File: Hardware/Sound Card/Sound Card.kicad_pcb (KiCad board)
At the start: 2 copper layers, 100 x 57.6 mm, 38 parts, among them J1 ICSP, J2 6502 Card Edge, J3 Conn_02x08_Odd_Even, J4 PORT A, J5 3.5mm TRS, U1 ATmega328P-A, U2 74HC245, U3 74HC245, U4 74HC138, U5 AY-3-8912, U6 LM386, X1 2 MHz, Y1 16MHz

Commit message: Add Wozmon
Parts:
- removed C10, C2, C5, C6: 100nF, Capacitor_SMD:C_0805_2012Metric
- removed C11: 470nF, Capacitor_SMD:C_0805_2012Metric
- removed C3, C4: 22pF, Capacitor_SMD:C_0805_2012Metric
- removed R4, R5, R6: 1k, Resistor_SMD:R_0805_2012Metric
- removed R7: 10, Resistor_SMD:R_0805_2012Metric
- removed U2, U3: 74HC245, Package_SO:SOIC-20W_7.5x12.8mm_P1.27mm
- removed U6: LM386, Package_SO:SOP-8_3.76x4.96mm_P1.27mm
- removed Y1: 16MHz, Crystal:Crystal_HC49-U_Vertical
- added JP1: SolderJumper_2_Bridged, Jumper:SolderJumper-2_P1.3mm_Bridged_RoundedPad1.0x1.5mm, F.Cu at (92.5, 110.2)
- D1: value 1N4001 -> D_Schottky; footprint Diode_SMD:D_SMA -> Diode_THT:D_DO-35_SOD27_P7.62mm_Horizontal
- J1: value ICSP -> Audio Out; footprint Connector_PinHeader_2.54mm:PinHeader_2x03_P2.54mm_Vertical -> Connector_JST:JST_XH_B2B-XH-A_1x02_P2.50mm_Vertical
- U1: value ATmega328P-A -> 65C22; footprint Package_QFP:TQFP-32_7x7mm_P0.8mm -> Package_DIP:DIP-40_W15.24mm_Socket_LongPads
- moved C1 48.9 mm to (86.1, 98.9)
- moved C8 44.6 mm to (86.1, 101.9)
- moved C9 44.6 mm to (86.1, 104.9)
- moved U1 44.4 mm to (43.6, 73.2)
- moved TP1 36.9 mm to (82.1, 99.2)
- moved TP2 36.9 mm to (82.1, 102.7)
- moved TP3 36.9 mm to (82.1, 106.2)
- moved R1 32.7 mm to (90.5, 98.8)
- moved R2 32.7 mm to (90.5, 101.8)
- moved R3 32.7 mm to (90.5, 104.8)
- moved J5 32.1 mm to (87.3, 79.5)
- moved U5 24.5 mm to (63.0, 73.2)
- moved J4 24.3 mm to (85.5, 110.7)
- moved X1 22.8 mm to (64.4, 119.3)
- moved J1 15.0 mm to (82.6, 89.0)
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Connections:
- C9 pad 2: Net-(U6-+) -> Net-(J1-Pin_1)
- D1 pad 1: GND -> Net-(D1-K)
- D1 pad 2: Net-(D1-A) -> IRQB
- J1 pad 1: MISO -> Net-(J1-Pin_1)
- J1 pad 2: VCC -> GND
- J2 pad IRQB: unconnected-(J2-PadIRQB) -> IRQB
- J2 pad RWB: MISO -> RWB
- J4 pad 11: unconnected-(J4-Pin_11-Pad11) -> CA1
- J4 pad 12: unconnected-(J4-Pin_12-Pad12) -> CA2
- J5 pad R: unconnected-(J5-PadR) -> GND
- J5 pad T: Net-(C11-Pad2) -> Net-(J1-Pin_1)
- TP2 pad 1: Net-(C11-Pad2) -> Net-(J1-Pin_1)
- U1 pad 1: PD3 -> GND
- U1 pad 10: PD6 -> BC1
- U1 pad 11: PD7 -> BDIR
- U1 pad 12: DDIR -> RESETB
- U1 pad 13: DEN0B -> unconnected-(U1-PB3-Pad13)
- U1 pad 14: DEN1B -> unconnected-(U1-PB4-Pad14)
- U1 pad 15: CSB -> unconnected-(U1-PB5-Pad15)
- U1 pad 16: MISO -> unconnected-(U1-PB6-Pad16)
- U1 pad 17: PHI2 -> unconnected-(U1-PB7-Pad17)
- U1 pad 18: VCC -> unconnected-(U1-CB1-Pad18)
- U1 pad 2: PD4 -> DA0
- U1 pad 20: Net-(U1-AREF) -> VCC
- U1 pad 21: GND -> Net-(D1-K)
- U1 pad 22: unconnected-(U1-ADC7-Pad22) -> RWB
- U1 pad 23: A0 -> CSB
- U1 pad 24: A1 -> VCC
- U1 pad 25: A2 -> PHI2
- U1 pad 26: A3 -> D7
- U1 pad 27: BC1 -> D6
- U1 pad 28: BDIR -> D5
- U1 pad 29: RESB -> D4
- U1 pad 3: GND -> DA1
- U1 pad 30: PD0 -> D3
- U1 pad 31: PD1 -> D2
- U1 pad 32: PD2 -> D1
- U1 pad 4: VCC -> DA2
- U1 pad 5: GND -> DA3
- U1 pad 6: VCC -> DA4
- U1 pad 7: Net-(U1-XTAL1/PB6) -> DA5
- U1 pad 8: Net-(U1-XTAL2/PB7) -> DA6
- U1 pad 9: PD5 -> DA7
- U5 pad 1: Net-(U5-CH_C) -> CHOUT
- U5 pad 16: RESB -> RESETB
- U5 pad 4: Net-(U5-CH_B) -> CHOUT
- U5 pad 5: Net-(U5-CH_A) -> CHOUT

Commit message: Cleanup
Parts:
- removed the J5 at (87.3, 79.5)
- added C3: 100nF, Capacitor_SMD:C_0805_2012Metric, F.Cu at (92.0, 91.0)
- added J4: Audio Out, 6502 Parts:SWITCHCRAFT_PJRAN1X1U02X, F.Cu at (87.3, 68.2)
- TP2: renamed from TP1; value Audio Raw -> Mixer
- renumbered C7 to C2, C8 to C4, C9 to C5, J2 to J1, J3 to J2, J4 to J3, J1 to J5, TP3 to TP1, TP2 to TP3, U4 to U2, U5 to U3

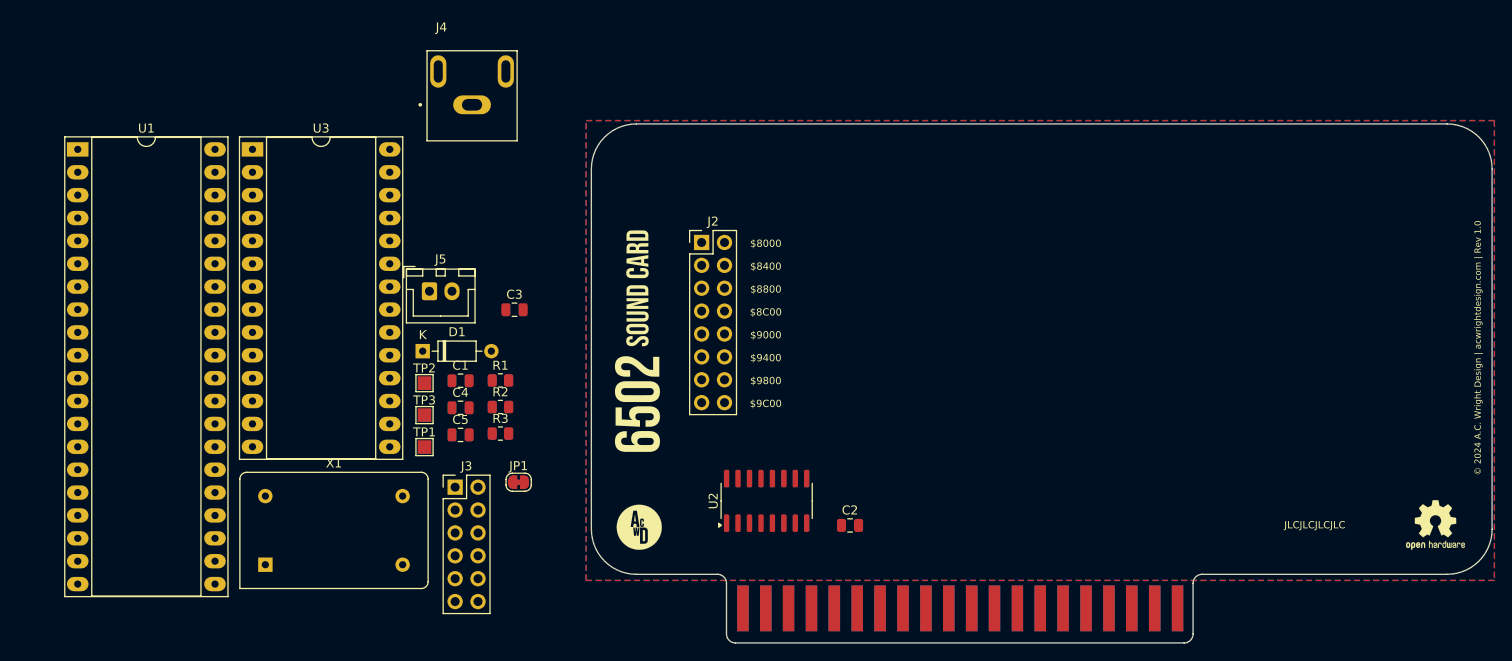
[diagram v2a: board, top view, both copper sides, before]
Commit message: Add Input Board and rework Debugger
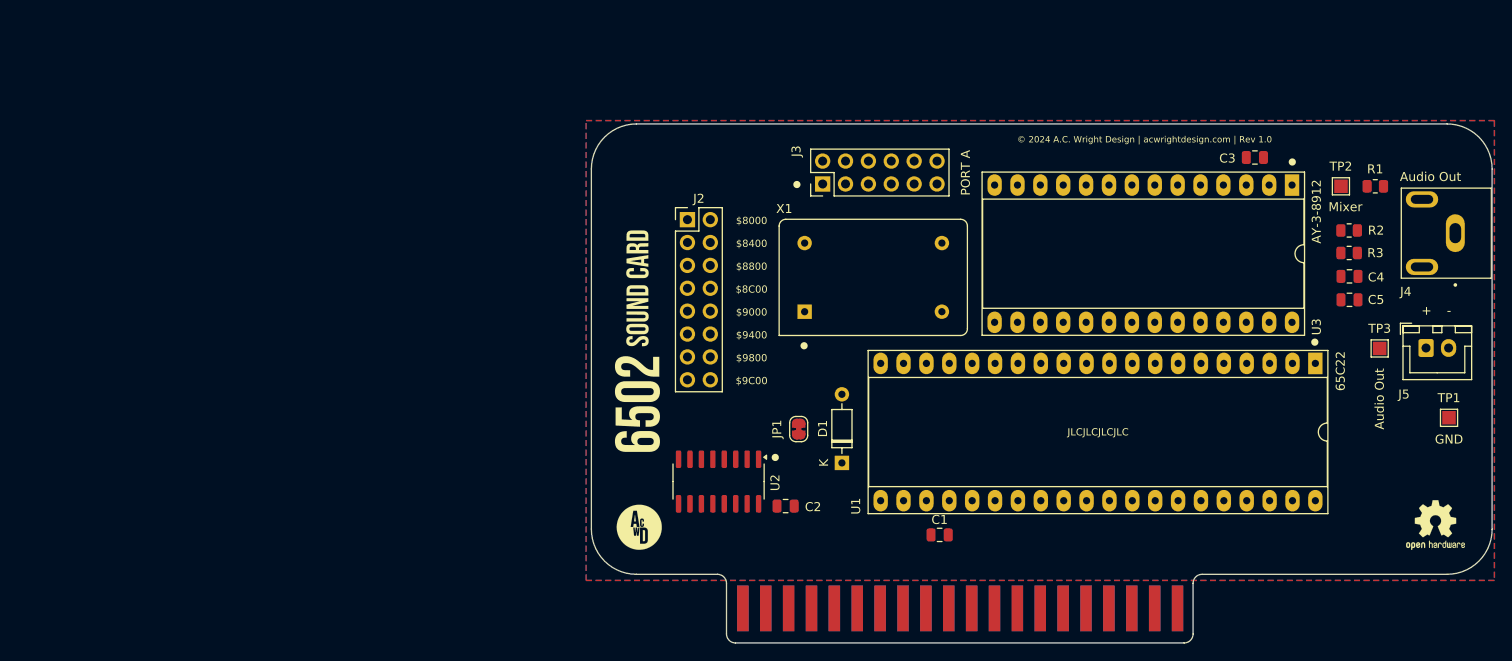
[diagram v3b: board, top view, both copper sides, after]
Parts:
- moved U1 139.4 mm to (181.0, 97.0), turned to -90 degrees
- moved U3 115.5 mm to (178.4, 77.2), turned to -90 degrees
- moved TP1 113.8 mm to (195.8, 103.0)
- moved J5 110.8 mm to (193.2, 95.2)
- moved J4 110.1 mm to (196.5, 82.5), turned to 90 degrees
- moved TP3 106.3 mm to (188.1, 95.3)
- moved TP2 104.1 mm to (183.8, 77.3)
- moved C5 99.8 mm to (184.8, 89.9)
- moved C4 99.8 mm to (184.8, 87.3), turned to 180 degrees
- moved R1 99.5 mm to (187.6, 77.3)
- moved R3 96.3 mm to (184.7, 84.7), turned to 180 degrees
- moved R2 96.2 mm to (184.7, 82.2)
- moved C3 83.9 mm to (174.2, 74.1)
- moved X1 66.1 mm to (124.3, 91.2)
- moved C1 55.9 mm to (139.2, 116.0)
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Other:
- board text added: "+"
- board text added: "-"

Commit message: Revise some boards
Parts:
- added J2: PHI2, Connector_PinHeader_2.54mm:PinHeader_1x02_P2.54mm_Vertical, F.Cu at (116.2, 74.4)
- renumbered J2 to J3, J3 to J4, J4 to J5, J5 to J6

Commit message: More PCBs
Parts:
- moved C2 11.2 mm to (111.2, 115.0)
- moved U2 2.58 mm to (113.2, 108.0), turned to 180 degrees
- moved C1 0.56 mm to (139.4, 115.5)
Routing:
- net VCC: track 0.00 -> 221.7 mm, vias 0 -> 10
- net PHI2: track 0.00 -> 78.7 mm, vias 0 -> 4
- net CA1: track 0.00 -> 74.9 mm, vias 0 -> 3
- net CA2: track 0.00 -> 74.0 mm, vias 0 -> 3
- net RESB: track 0.00 -> 57.1 mm, vias 0 -> 3
- net CSB: track 0.00 -> 54.0 mm, vias 0 -> 1
- net PA7: track 0.00 -> 42.2 mm, vias 0 -> 1
- net Net-(J2-Pin_2): track 0.00 -> 41.2 mm, vias 0 -> 2
- net /$8000: track 0.00 -> 36.4 mm
- net PA6: track 0.00 -> 35.5 mm, vias 0 -> 1
- net A10: track 0.00 -> 33.3 mm, vias 0 -> 3
- net CHOUT: track 0.00 -> 32.7 mm
- net /$8400: track 0.00 -> 32.3 mm
- net A11: track 0.00 -> 32.1 mm, vias 0 -> 3
- net IRQB: track 0.00 -> 30.1 mm
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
